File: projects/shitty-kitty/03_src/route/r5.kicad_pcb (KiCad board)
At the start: 4 copper layers, 130 x 75 mm, 82 parts, among them J1 DC-005C-20A 12V, J2 TYPE-C-31-M-12, J3 ELECTRODES INNER, J4 ELECTRODES OUTER, J5 MOTOR NEMA17, J6 ENDSTOP TERM, J8 HOST 1x6, Q1 AOD4185 revpol, SW1 TS-1187A BOOT, SW2 TS-1187A RESET, U1 ESP32-S3-WROOM-1-N8R2, U2 TMC2209-LA-T, U3 MPR121QR2 0x5A, U4 MPR121QR2 0x5B, U5 MPR121QR2 0x5C, U6 MPR121QR2 0x5D, U7 LIS2DH12TR, U8 AP63205WU-7, U9 AMS1117-3.3

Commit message: shitty-kitty: fab-floor pin for KRT (no advanced-via escalation), honest hole floors (h2h 0.3/holeclr 0.2), ELEC/3V3 width floors match router grading, route_surgery tool, stitcher fine-pitch GND rescue + via-pad joins
Co-Authored-By: Claude Fable 5 <noreply@anthropic.com>
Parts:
- moved C12 13.0 mm to (154.0, 104.5)
- moved R9 11.7 mm to (149.5, 108.0)
- moved J5 7.00 mm to (176.0, 91.0)
- moved C26 6.52 mm to (154.0, 101.5)
- moved R20 6.04 mm to (67.0, 74.5)
- moved J1 6.00 mm to (166.5, 70.0)
- moved C41 5.00 mm to (167.0, 88.5)
- moved C17 4.53 mm to (166.0, 110.0)
- moved R10 4.53 mm to (166.0, 107.0)
- moved R11 4.53 mm to (166.0, 113.0)
- moved C13 3.54 mm to (154.0, 107.5)
- moved C16 3.54 mm to (154.0, 110.5)
- moved J6 3.50 mm to (176.0, 113.0)
- moved J3 3.00 mm to (61.0, 54.5)
- moved C30 2.55 mm to (61.0, 69.5)
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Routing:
- net SCL: track 105.9 -> 147.1 mm, vias 8 -> 17
- net OUTER1: track 0.00 -> 27.2 mm
- net ACC_INT: track 0.00 -> 23.7 mm
- net INNER2: track 0.00 -> 21.2 mm
- net OUTER8: track 0.00 -> 21.1 mm
- net INNER12: track 0.00 -> 18.5 mm
- net OUTER11: track 0.00 -> 16.5 mm
- net INNER5: track 0.00 -> 16.4 mm
- net OUTER6: track 0.00 -> 14.1 mm, vias 0 -> 2
- net INNER6: track 0.00 -> 13.6 mm, vias 0 -> 2
- net 5V: track 74.2 -> 87.8 mm, vias 2 -> 5
- net BRB: track 0.00 -> 13.6 mm
- net OUTER12: track 0.00 -> 13.5 mm, vias 0 -> 2
- net OUTER7: track 0.00 -> 12.9 mm, vias 0 -> 2
- net INNER11: track 0.00 -> 12.8 mm, vias 0 -> 2
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
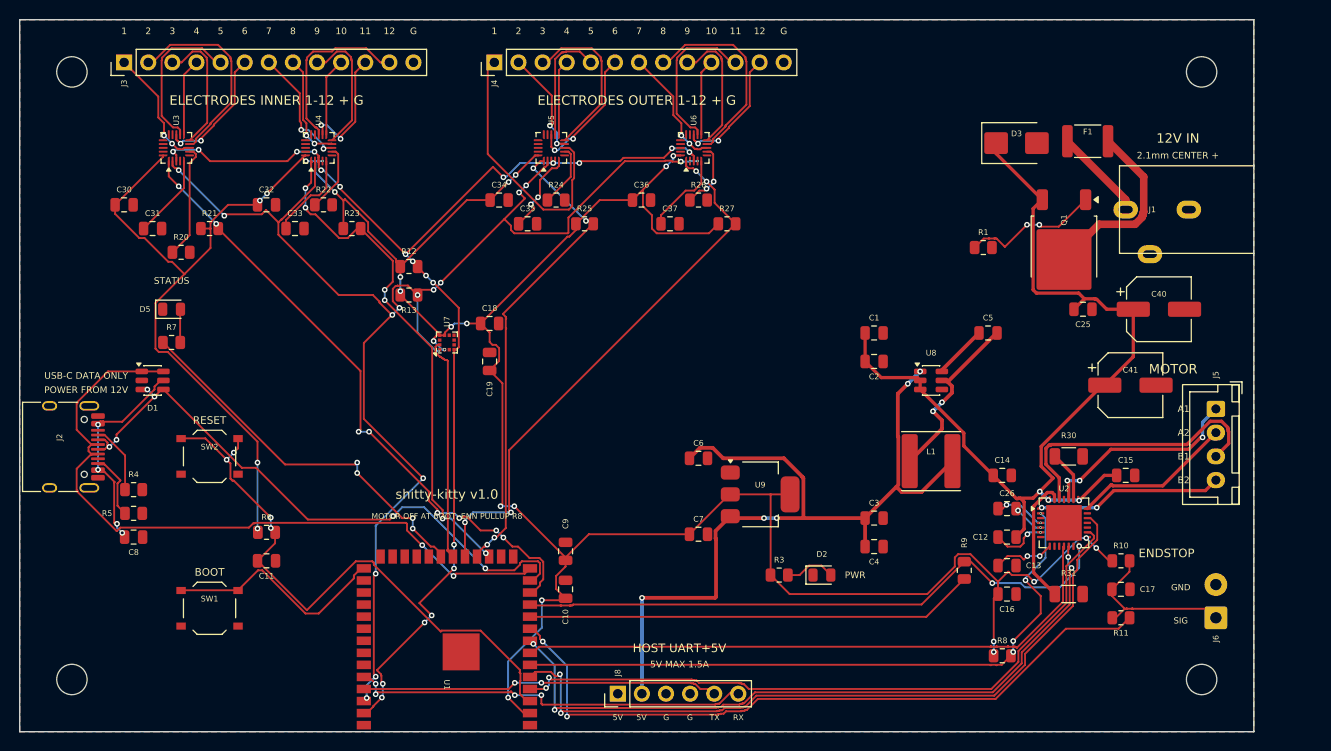
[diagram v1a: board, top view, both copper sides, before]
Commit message: shitty-kitty: WIP CHECKPOINT (not a gate) — routing surgery mid-flight, 18 DRC violations remain (6 clearance/5 hole_clr/6 h2h/1 conn_width from the SDA-via relocation), 0 unconnected. Route-surgery tooling: route_taps/route_unlock/lift_floors. Agent died on Fable credit wall; preserving work
Co-Authored-By: Claude Fable 5 <noreply@anthropic.com>
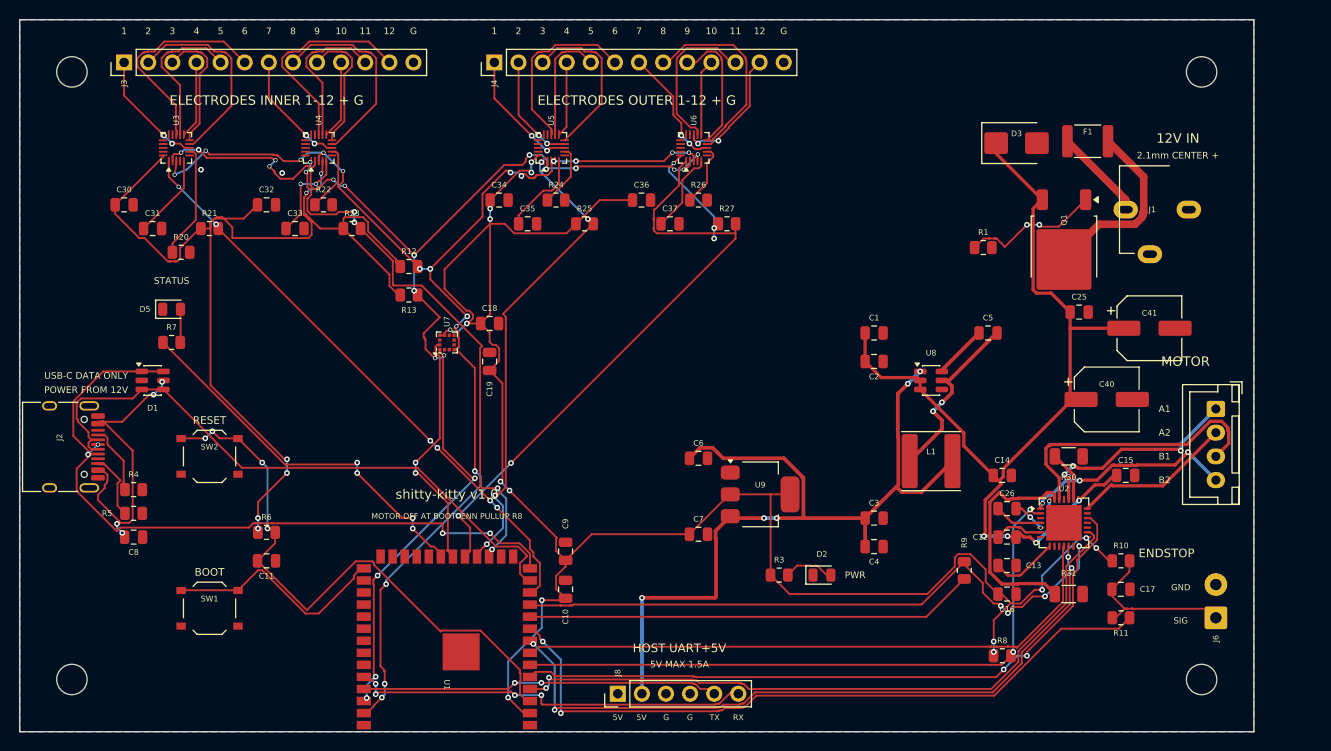
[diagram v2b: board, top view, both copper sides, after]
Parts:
- moved C40 11.0 mm to (164.5, 90.0)
- moved C41 6.32 mm to (169.0, 82.5)
- moved C25 0.50 mm to (161.6, 80.8)
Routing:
- net 3V3: track 309.8 -> 324.3 mm, vias 26 -> 24
- net OUTER1: track 27.2 -> 13.6 mm, vias 0 -> 2
- net SCL: track 147.1 -> 134.0 mm, vias 17 -> 20
- net BRB: track 13.6 -> 23.8 mm
- net INNER8: track 11.4 -> 20.9 mm, vias 2 -> 0
- net USB_VBUS: track 22.4 -> 31.8 mm
- net INNER6: track 13.6 -> 22.7 mm, vias 2 -> 0
- net MPR_IRQ4: track 58.4 -> 65.4 mm, vias 4 -> 2
- net DIR: track 77.9 -> 71.9 mm
- net SDA: track 125.7 -> 131.3 mm
- net OUTER6: track 14.1 -> 19.0 mm, vias 2 -> 0
- net MPR_IRQ1: track 67.1 -> 62.2 mm, vias 8 -> 6
- net VIN_12V: track 98.9 -> 103.7 mm, vias 3 -> 5
- net INNER12: track 18.5 -> 22.6 mm
- net MPR_IRQ2: track 54.2 -> 57.6 mm
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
